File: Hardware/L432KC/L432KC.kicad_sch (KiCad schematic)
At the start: 47 parts, among them J1 L4_G4, J2 USB_B_Micro, J3 JTAG, J4 3v3, J5 GND, J6 Conn_01x09, J7 Conn_01x08, J8 TVCC, J9 LogicAna, U1 TXS0108EPW, U2 AD8531ARTZ, U3 NUCLEO-L432KC, U4 SRV05-4, U5 SRV05-4, U6 SRV05-4

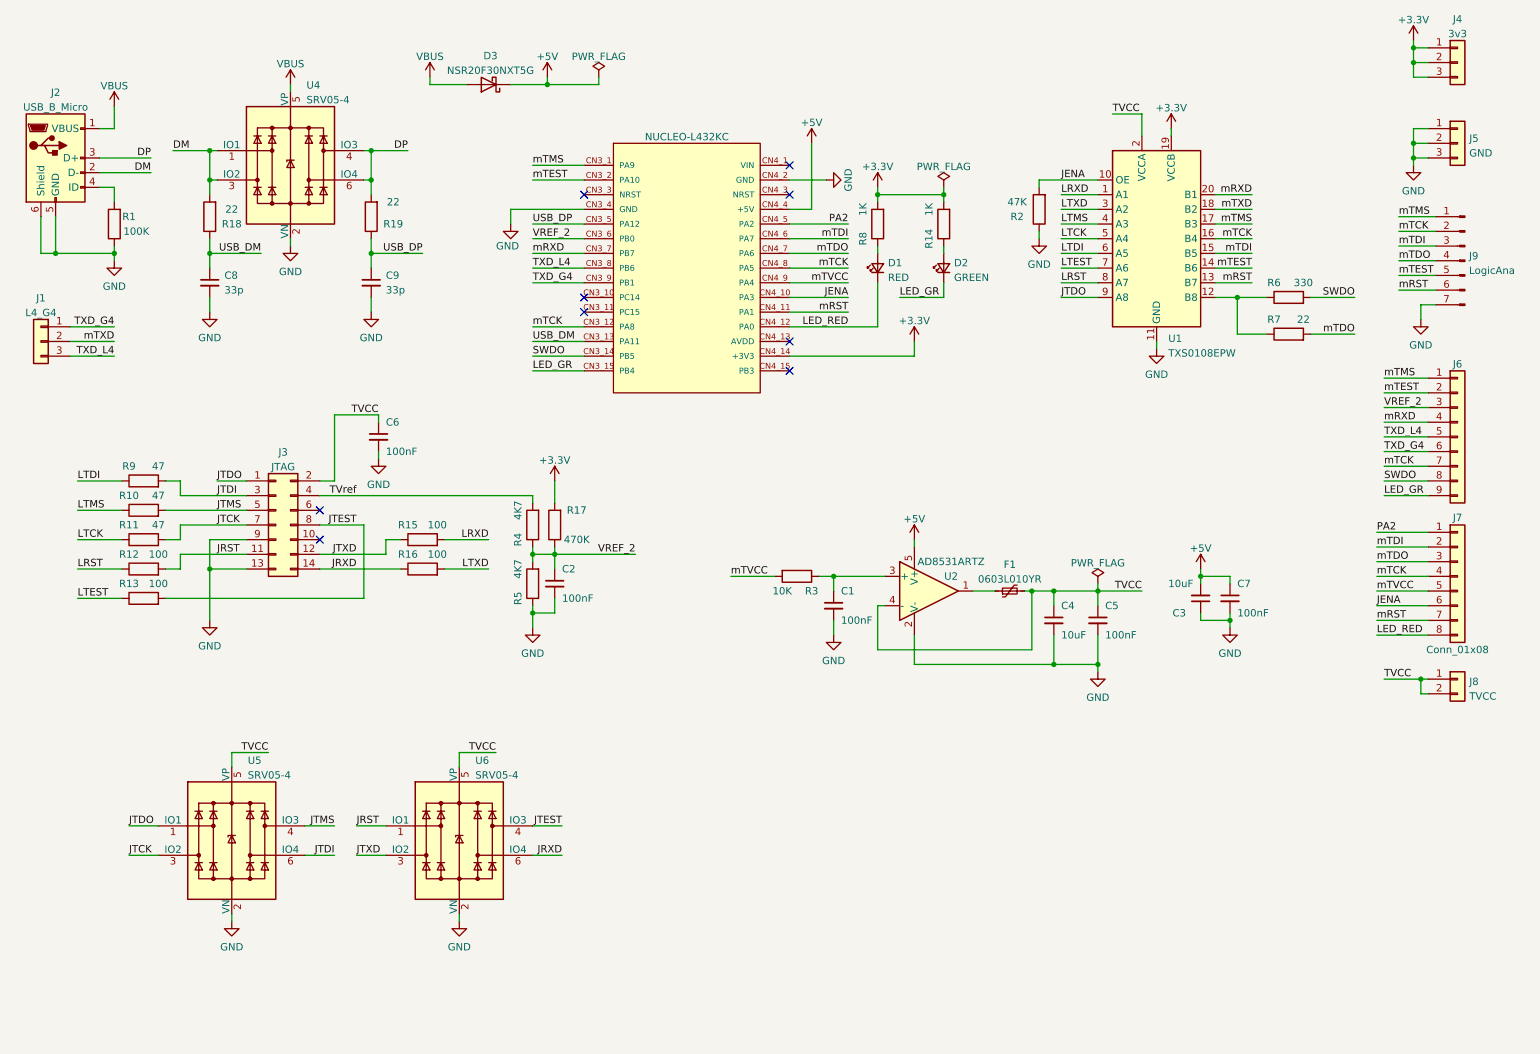
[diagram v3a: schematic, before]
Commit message: Swapped LRXD and LTXD on both prototype boards.
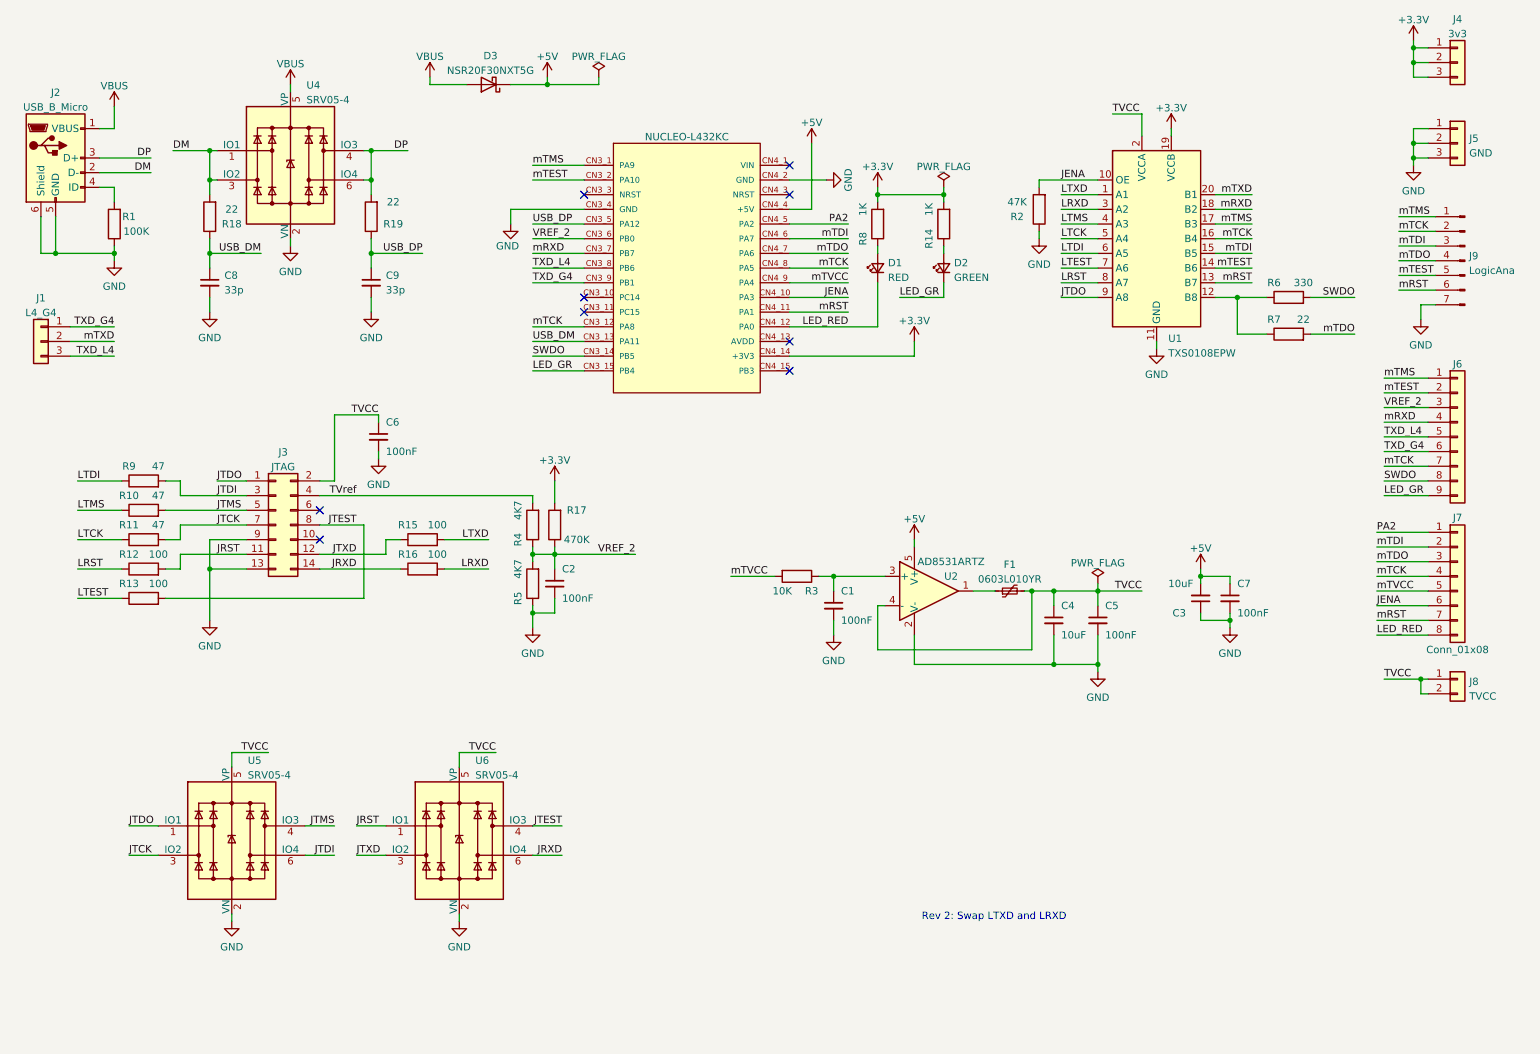
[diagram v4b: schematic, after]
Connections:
- net LRXD: now also R16.2, U1.3 (A2); no longer R15.2, U1.1 (A1)
- net LTXD: now also R15.2, U1.1 (A1); no longer R16.2, U1.3 (A2)
- net mRXD: now also U1.18 (B2); no longer U1.20 (B1)
- net mTXD: now also U1.20 (B1); no longer U1.18 (B2)
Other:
- note added: "Rev 2: Swap LTXD and LRXD"
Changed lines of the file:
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@@
 (kicad_sch (version 20211123) (generator eeschema)
   (paper "A4")
+  (title_block
+    (date "2022-08-18")
+    (rev "2")
+  )
   (junction (at 55.88 54.61) (diameter 0) (color 0 0 0 0)
   )
@@
     (stroke (width 0) (type default) (color 0 0 0 0))
   )
+  (text "Rev 2: Swap LTXD and LRXD" (at 179.07 170.18 0)
+    (effects (font (size 1.27 1.27)) (justify left bottom))
+  )
   (label "LTCK" (at 203.2 52.07 0)
     (effects (font (size 1.27 1.27)) (justify left bottom))
@@
     (effects (font (size 1.27 1.27)) (justify left bottom))
   )
-  (label "LTXD" (at 203.2 46.99 0)
+  (label "LTXD" (at 203.2 44.45 0)
     (effects (font (size 1.27 1.27)) (justify left bottom))
   )
@@
     (effects (font (size 1.27 1.27)) (justify right bottom))
   )
-  (label "LTXD" (at 104.14 109.22 180)
+  (label "LTXD" (at 104.14 104.14 180)
     (effects (font (size 1.27 1.27)) (justify right bottom))
   )
@@
     (effects (font (size 1.27 1.27)) (justify right bottom))
   )
-  (label "mRXD" (at 236.22 44.45 180)
+  (label "mRXD" (at 236.22 46.99 180)
     (effects (font (size 1.27 1.27)) (justify right bottom))
   )
@@
     (effects (font (size 1.27 1.27)) (justify left bottom))
   )
-  (label "mTXD" (at 236.22 46.99 180)
+  (label "mTXD" (at 236.22 44.45 180)
     (effects (font (size 1.27 1.27)) (justify right bottom))
   )
@@
     (effects (font (size 1.27 1.27)) (justify left bottom))
   )
-  (label "LRXD" (at 104.14 104.14 180)
+  (label "LRXD" (at 104.14 109.22 180)
     (effects (font (size 1.27 1.27)) (justify right bottom))
   )
@@
     (effects (font (size 1.27 1.27)) (justify left bottom))
   )
-  (label "LRXD" (at 203.2 44.45 0)
-    (effects (font (size 1.27 1.27)) (justify left bottom))
-  )
+  (label "LRXD" (at 203.2 46.99 0)
+    (effects (font (size 1.27 1.27)) (justify left bottom))
+  )

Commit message: Review of ESD protection for Development boards.
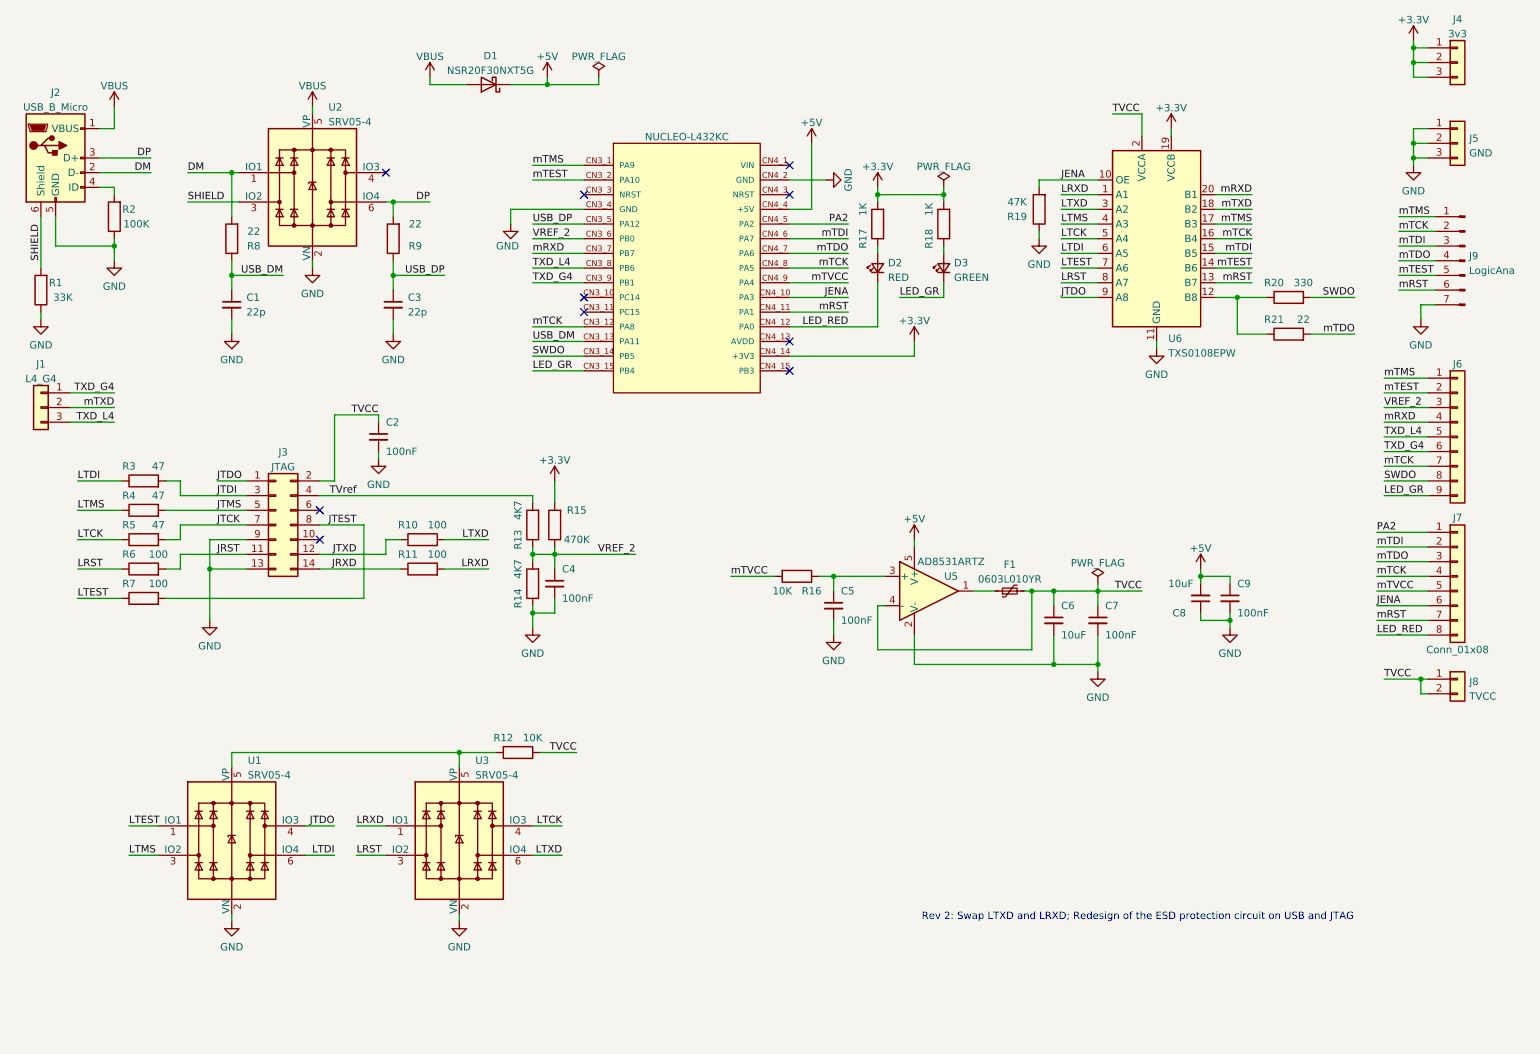
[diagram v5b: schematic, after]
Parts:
- added R1: 33K, Resistor_SMD:R_0603_1608Metric_Pad0.98x0.95mm_HandSolder, symbol Device:R
- added R12: 10K, Resistor_SMD:R_0603_1608Metric_Pad0.98x0.95mm_HandSolder, symbol Device:R
- C1: renamed from C8; value 33p -> 22p
- C3: renamed from C9; value 33p -> 22p
- renumbered C6 to C2, C2 to C4, C1 to C5, C4 to C6, C5 to C7, C3 to C8, C7 to C9, D3 to D1, D1 to D2, D2 to D3, R15 to R10, R16 to R11, R4 to R13, R5 to R14, R17 to R15, R3 to R16, R8 to R17, R14 to R18, R2 to R19, R1 to R2, R6 to R20, R7 to R21, R9 to R3, R10 to R4, R11 to R5, R12 to R6, R13 to R7, R18 to R8, R19 to R9, U5 to U1, U4 to U2, U6 to U3, U3 to U4, U2 to U5, U1 to U6
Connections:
- net DM: no longer U2.3 (IO2)
- net DP: no longer U2.4 (IO3)
- net GND: now also R1.1; no longer J2.6 (Shield)
- net JRST: no longer U3.1 (IO1)
- net JRXD: no longer U3.6 (IO4)
- net JTCK: no longer U1.3 (IO2)
- net JTDI: no longer U1.6 (IO4)
- net JTDO: now also U1.4 (IO3); no longer U1.1 (IO1)
- net JTEST: no longer U3.4 (IO3)
- net JTMS: no longer U1.4 (IO3)
- net JTXD: no longer U3.3 (IO2)
- net LRST: now also U3.3 (IO2)
- net LRXD: now also U3.1 (IO1), U6.1 (A1); no longer U6.3 (A2)
- net LTCK: now also U3.4 (IO3)
- net LTDI: now also U1.6 (IO4)
- net LTEST: now also U1.1 (IO1)
- net LTMS: now also U1.3 (IO2)
- net LTXD: now also U3.6 (IO4), U6.3 (A2); no longer U6.1 (A1)
- net TVCC: now also R12.1; no longer U1.5 (VP), U3.5 (VP)
- net mRXD: now also U6.20 (B1); no longer U6.18 (B2)
- net mTXD: now also U6.18 (B2); no longer U6.20 (B1)
- new net: R12.2, U1.5 (VP), U3.5 (VP)
- new net SHIELD: J2.6 (Shield), R1.2, U2.3 (IO2)
- no-connect marks 9 -> 10
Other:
- note added: "Rev 2: Swap LTXD and LRXD; Redesign of the ESD protection circuit on USB and JTAG"
- note removed: "Rev 2: Swap LTXD and LRXD"
- moved on the sheet: C1, C3, J1, R2, R8, R9, U2

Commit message: Changed TXS0108 for TXB0304. for lower impedance. Using ESD protection of those parts.
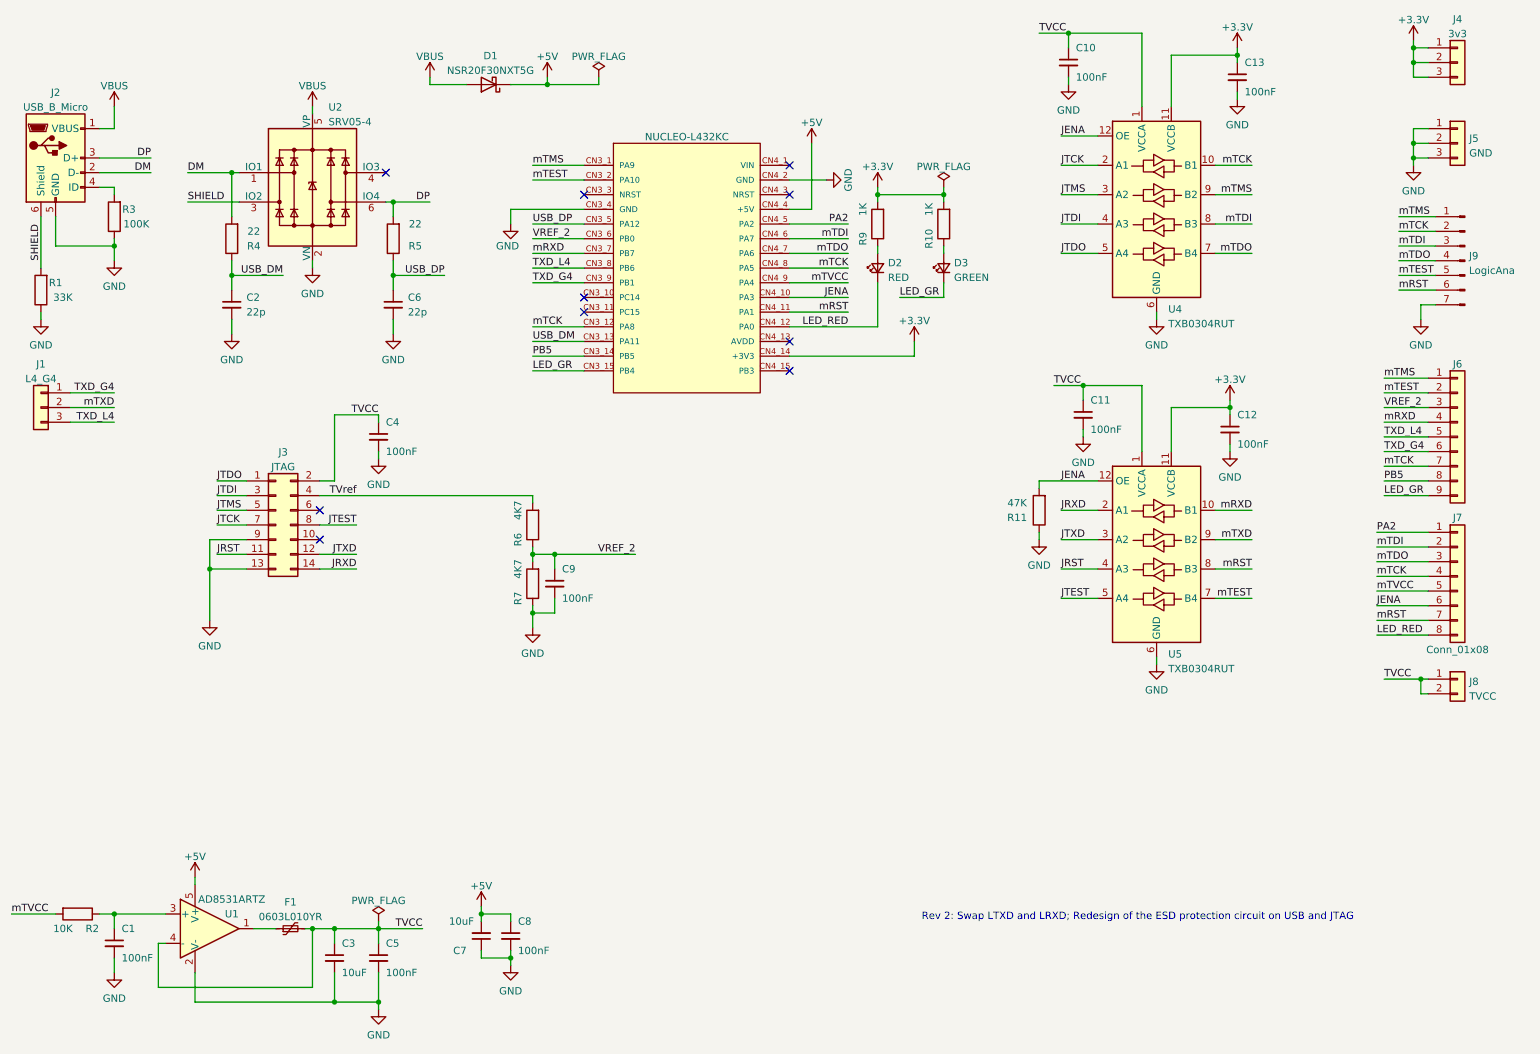
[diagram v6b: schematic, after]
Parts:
- removed R10, R11, R6, R7: 100, Resistor_SMD:R_0603_1608Metric_Pad0.98x0.95mm_HandSolder, symbol Device:R
- removed R12: 10K, Resistor_SMD:R_0603_1608Metric_Pad0.98x0.95mm_HandSolder, symbol Device:R
- removed R15: 470K, Resistor_SMD:R_0603_1608Metric_Pad0.98x0.95mm_HandSolder, symbol Device:R
- removed R20: 330, Resistor_SMD:R_0603_1608Metric_Pad0.98x0.95mm_HandSolder, symbol Device:R
- removed R21: 22, Resistor_SMD:R_0603_1608Metric_Pad0.98x0.95mm_HandSolder, symbol Device:R
- removed R3, R4, R5: 47, Resistor_SMD:R_0603_1608Metric_Pad0.98x0.95mm_HandSolder, symbol Device:R
- removed U1, U3: SRV05-4, Package_TO_SOT_SMD:SOT-23-6_Handsoldering, symbol Power_Protection:SRV05-4
- added C10, C11, C12, C13: 100nF, Capacitor_SMD:C_0603_1608Metric_Pad1.08x0.95mm_HandSolder, symbol Device:C_Small
- added U4: TXB0304RUT, Package_DFN_QFN:Texas_R_PUQFN-N12, symbol Logic_LevelTranslator:TXB0304RUT
- U5: renamed from U6; value TXS0108EPW -> TXB0304RUT; footprint Package_SO:TSSOP-20_4.4x6.5mm_P0.65mm -> Package_DFN_QFN:Texas_R_PUQFN-N12; symbol Logic_LevelTranslator:TXS0108EPW -> Logic_LevelTranslator:TXB0304RUT
- renumbered C5 to C1, C1 to C2, C6 to C3, C2 to C4, C7 to C5, C3 to C6, C8 to C7, C9 to C8, C4 to C9, R18 to R10, R19 to R11, R16 to R2, R2 to R3, R8 to R4, R9 to R5, R13 to R6, R14 to R7, R17 to R9, U5 to U1, U4 to U3
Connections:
- net LRST is gone; now on net mRST: U5.8 (B3)
- net LRXD is gone; now on net TVCC: U5.1 (VCCA)
- net LTCK is gone; now on net JTEST: U5.5 (A4)
- net LTDI is gone; now on net GND: U5.6 (GND)
- net LTEST is gone; now on net mTEST: U5.7 (B4)
- net LTMS is gone; now on net JRST: U5.4 (A3)
- net LTXD is gone; now on net JTXD: U5.3 (A2)
- net +3.3V: now also U5.11 (VCCB), C12.1, C13.1, U4.11 (VCCB); no longer U5.19 (VCCB)
- net GND: now also C10.2, C11.2, C12.2, C13.2, U4.6 (GND); no longer U5.11 (GND)
- net JENA: now also U5.12 (OE), U4.12 (OE); no longer U5.10 (OE)
- net JRXD: now also U5.2 (A1)
- net JTCK: now also U4.2 (A1)
- net JTDI: now also U4.4 (A3)
- net JTDO: now also U4.5 (A4); no longer U5.9 (A8)
- net JTMS: now also U4.3 (A2)
- net TVCC: now also C10.1, C11.1, U4.1 (VCCA); no longer U5.2 (VCCA)
- net mRST: no longer U5.13 (B7)
- net mRXD: now also U5.10 (B1); no longer U5.20 (B1)
- net mTCK: now also U4.10 (B1); no longer U5.16 (B4)
- net mTDI: now also U4.8 (B3); no longer U5.15 (B5)
- net mTDO: now also U4.7 (B4)
- net mTEST: no longer U5.14 (B6)
- net mTMS: now also U4.9 (B2); no longer U5.17 (B3)
- net mTXD: now also U5.9 (B2); no longer U5.18 (B2)
- net SWDO renamed PB5
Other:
- moved on the sheet: C1, C3, C5, C7, C8, F1, R11, R2, U1, U5
